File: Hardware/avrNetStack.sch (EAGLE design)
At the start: 38 parts, among them IC1 MEGA32-P, IC2 ENC28J60SP, Q1 16M, Q2 25M

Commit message: Fixed Hardware Problem.
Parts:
- added C1, C3: 100n, resistor:C-EU025-030X050
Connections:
- new net N$34: C3.1, IC1.AREF
- net GND: now also C1.1, C3.2, IC1.AGND
- net VCC: now also C1.2, IC1.AVCC
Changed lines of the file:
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@@
 <part name="L1" library="resistor" deviceset="L-EU" device="0204/7" value="10u"/>
 <part name="VDD10" library="supply1" deviceset="VDD" device=""/>
+<part name="C1" library="resistor" deviceset="C-EU" device="025-030X050" value="100n"/>
+<part name="C3" library="resistor" deviceset="C-EU" device="025-030X050" value="100n"/>
+<part name="P+6" library="supply1" deviceset="VCC" device=""/>
+<part name="GND19" library="supply1" deviceset="GND" device=""/>
+<part name="GND20" library="supply1" deviceset="GND" device=""/>
 </parts>
 <sheets>
@@
 <instance part="L1" gate="G$1" x="337.82" y="68.58"/>
 <instance part="VDD10" gate="G$1" x="337.82" y="58.42" rot="R180"/>
+<instance part="C1" gate="G$1" x="45.72" y="96.52" rot="R180"/>
+<instance part="C3" gate="G$1" x="35.56" y="101.6" rot="R270"/>
+<instance part="P+6" gate="VCC" x="38.1" y="99.06" rot="R90"/>
+<instance part="GND19" gate="1" x="38.1" y="93.98" rot="R270"/>
+<instance part="GND20" gate="1" x="27.94" y="101.6" rot="R270"/>
 </instances>
 <busses>
@@
 <junction x="154.94" y="78.74"/>
 </segment>
+<segment>
+<pinref part="P+6" gate="VCC" pin="VCC"/>
+<wire x1="40.64" y1="99.06" x2="43.18" y2="99.06" width="0.1524" layer="91"/>
+<wire x1="43.18" y1="99.06" x2="43.18" y2="101.6" width="0.1524" layer="91"/>
+<pinref part="IC1" gate="G$1" pin="AVCC"/>
+<wire x1="50.8" y1="99.06" x2="48.26" y2="99.06" width="0.1524" layer="91"/>
+<wire x1="48.26" y1="99.06" x2="48.26" y2="101.6" width="0.1524" layer="91"/>
+<pinref part="C1" gate="G$1" pin="2"/>
+<wire x1="48.26" y1="101.6" x2="45.72" y2="101.6" width="0.1524" layer="91"/>
+<wire x1="43.18" y1="101.6" x2="45.72" y2="101.6" width="0.1524" layer="91"/>
+<junction x="45.72" y="101.6"/>
+</segment>
 </net>
 <net name="GND" class="0">
@@
 <wire x1="152.4" y1="63.5" x2="154.94" y2="63.5" width="0.1524" layer="91"/>
 <junction x="154.94" y="63.5"/>
+</segment>
+<segment>
+<pinref part="C3" gate="G$1" pin="2"/>
+<pinref part="GND20" gate="1" pin="GND"/>
+</segment>
+<segment>
+<pinref part="IC1" gate="G$1" pin="AGND"/>
+<wire x1="50.8" y1="96.52" x2="48.26" y2="96.52" width="0.1524" layer="91"/>
+<wire x1="48.26" y1="96.52" x2="48.26" y2="93.98" width="0.1524" layer="91"/>
+<pinref part="C1" gate="G$1" pin="1"/>
+<wire x1="48.26" y1="93.98" x2="45.72" y2="93.98" width="0.1524" layer="91"/>
+<pinref part="GND19" gate="1" pin="GND"/>
+<wire x1="40.64" y1="93.98" x2="45.72" y2="93.98" width="0.1524" layer="91"/>
+<junction x="45.72" y="93.98"/>
 </segment>
 </net>
@@
 </segment>
 </net>
+<net name="N$34" class="0">
+<segment>
+<pinref part="IC1" gate="G$1" pin="AREF"/>
+<wire x1="50.8" y1="101.6" x2="50.8" y2="104.14" width="0.1524" layer="91"/>
+<wire x1="50.8" y1="104.14" x2="40.64" y2="104.14" width="0.1524" layer="91"/>
+<wire x1="40.64" y1="104.14" x2="40.64" y2="101.6" width="0.1524" layer="91"/>
+<pinref part="C3" gate="G$1" pin="1"/>
+<wire x1="40.64" y1="101.6" x2="38.1" y2="101.6" width="0.1524" layer="91"/>
+</segment>
+</net>

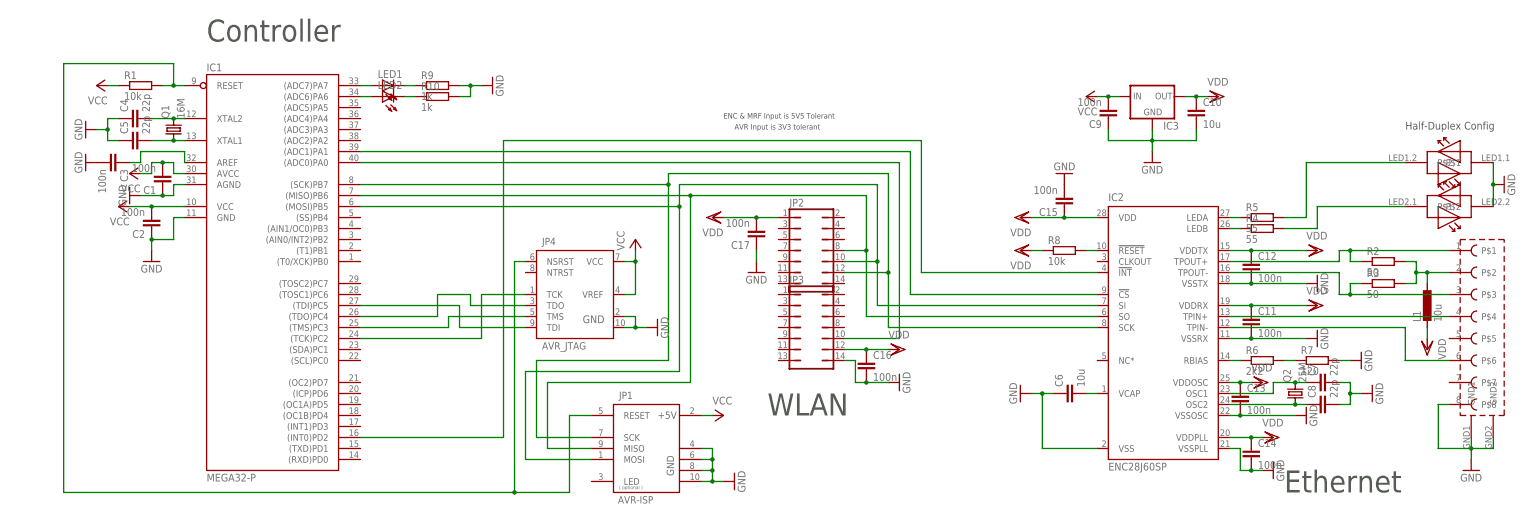
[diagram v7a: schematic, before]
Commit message: Fixed WiFi int pin.
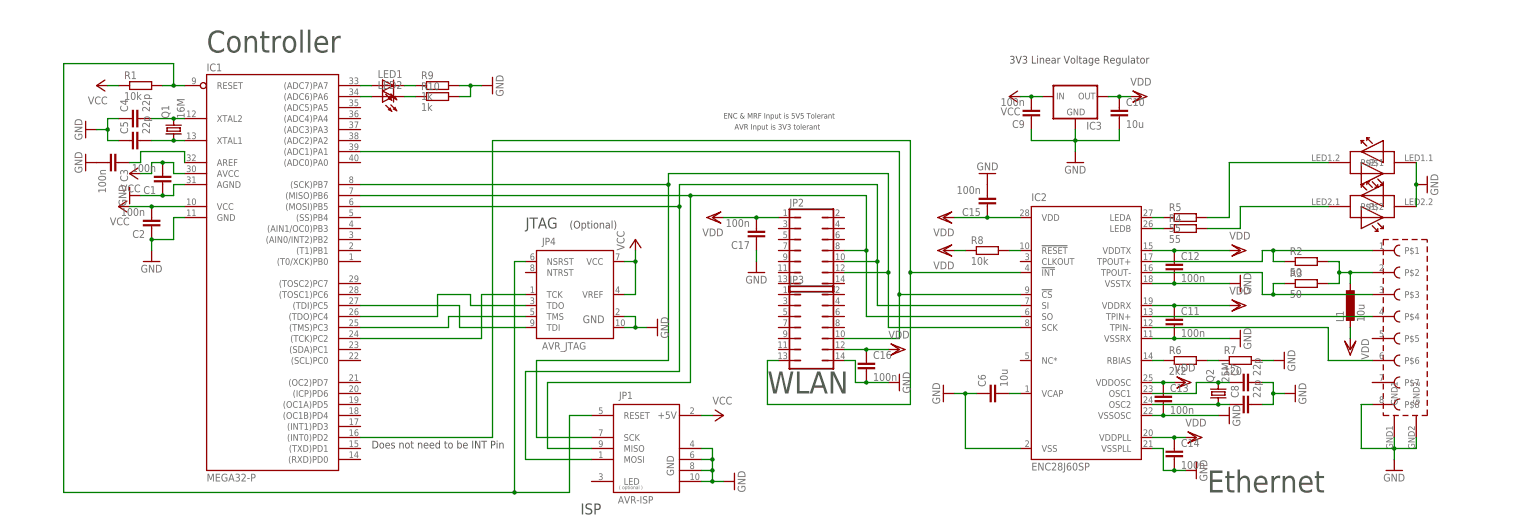
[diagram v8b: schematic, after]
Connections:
- removed net N$12: IC1.(ADC0)PA0, JP3.10
- net N$13: now also JP3.10
- net N$2: now also JP3.13
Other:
- note added: "(Optional)"
- note added: "3V3 Linear Voltage Regulator"
- note added: "Does not need to be INT Pin"
- note added: "ISP"
- note added: "JTAG"
- note removed: "Half-Duplex Config"
- moved on the sheet: C10, C11, C12, C13, C14, C15, C6, C7, C8, C9, IC2, IC3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
